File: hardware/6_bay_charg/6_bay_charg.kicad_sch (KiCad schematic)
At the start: 0 parts

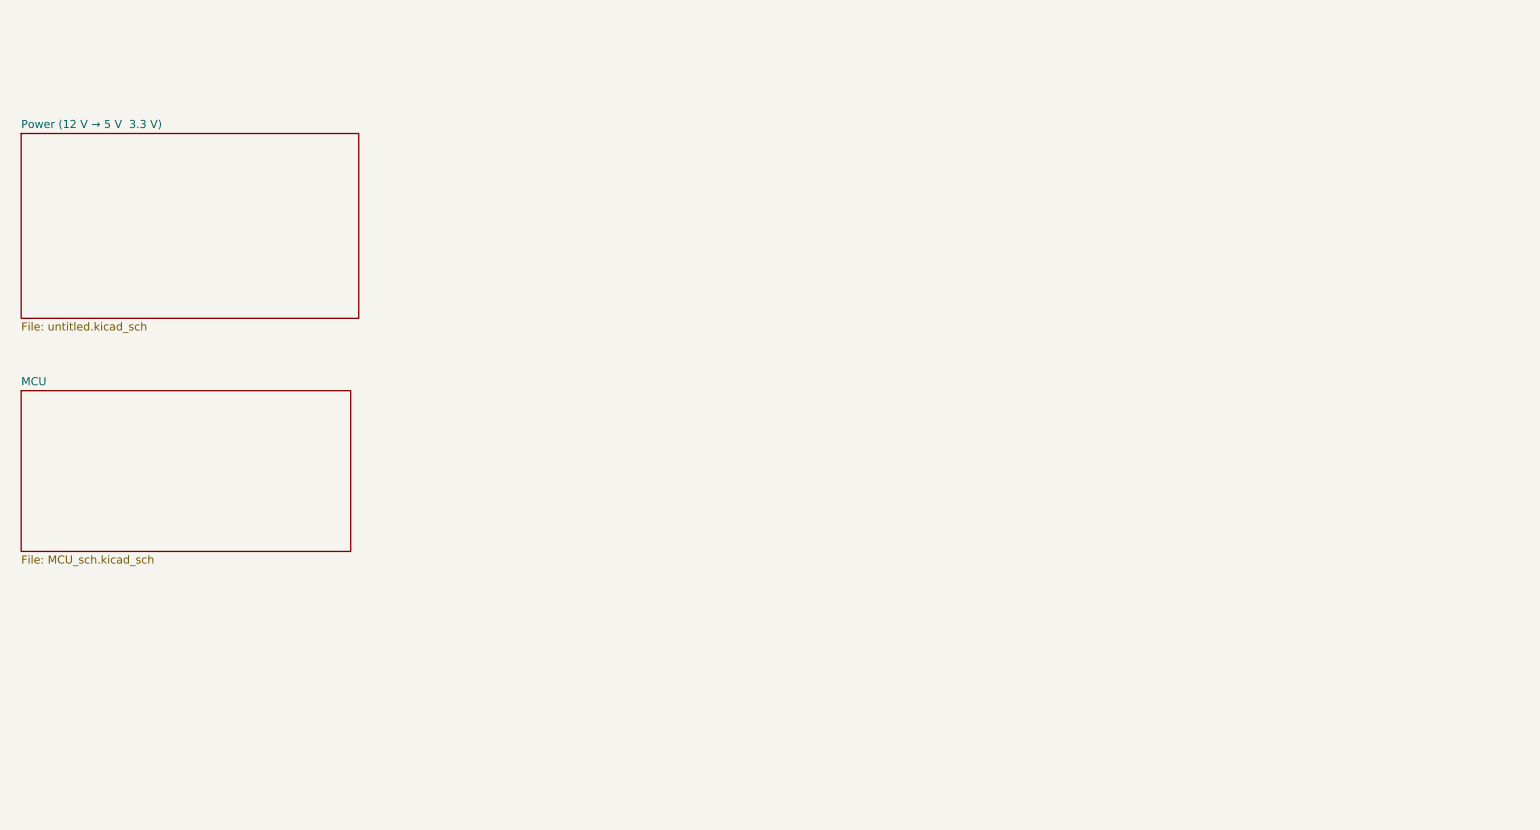
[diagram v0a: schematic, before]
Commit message: adding 3.3v buck sch + bay1
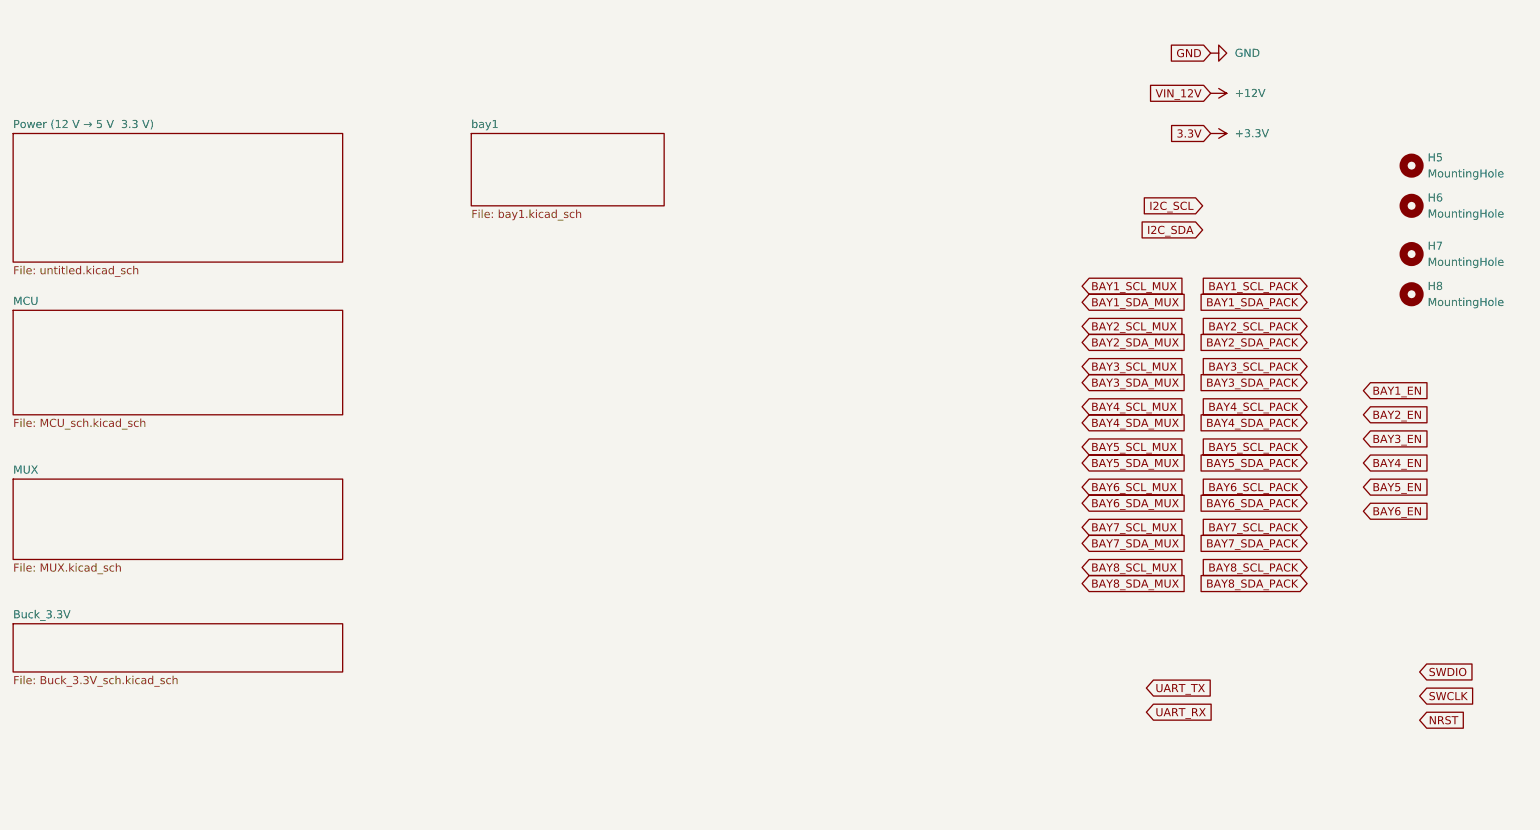
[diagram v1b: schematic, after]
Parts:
- added H5, H6, H7, H8: MountingHole, MountingHole:MountingHole_2.2mm_M2, symbol Mechanical:MountingHole
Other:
- added sheet Buck_3.3V (Buck_3.3V_sch.kicad_sch)
- added sheet MUX (MUX.kicad_sch)
- added sheet bay1 (bay1.kicad_sch)
- company: (none) -> EOS Positioning Systems

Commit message: Update KiCad schematics: dual GPIO charge/discharge per bay
- Refactored bay power control logic
- Separated GPIOs for charge and discharge paths
- Added safe idle state with hardware interlock
- Improved overall safety and control clarity
- Updated and exported schematic PDF plots
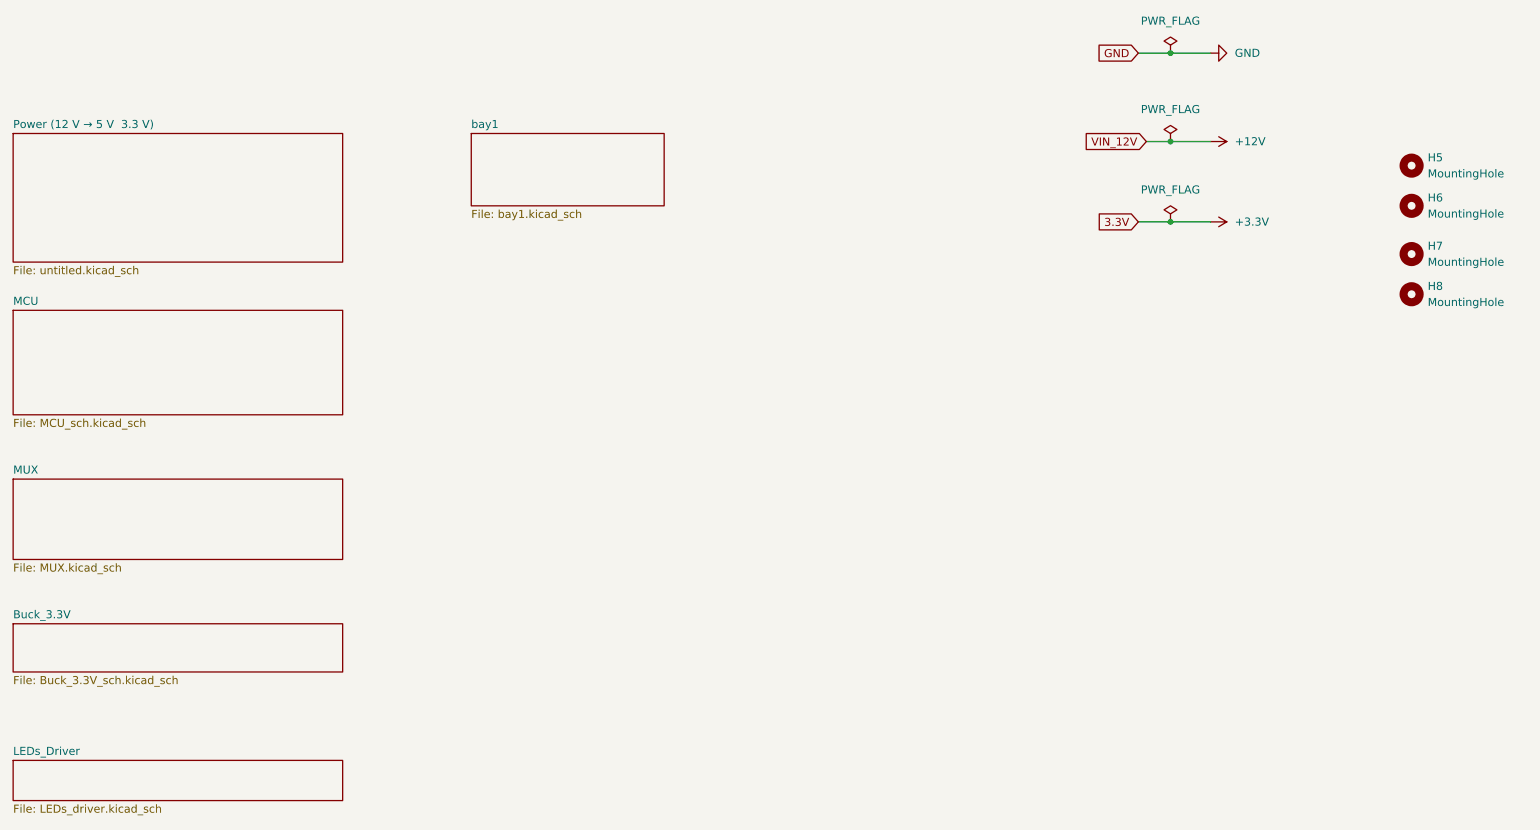
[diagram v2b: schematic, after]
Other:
- added sheet LEDs_Driver (LEDs_driver.kicad_sch)

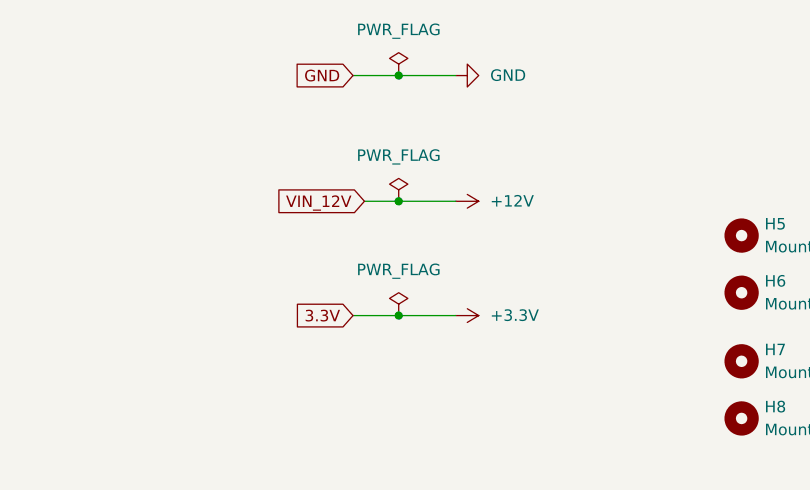
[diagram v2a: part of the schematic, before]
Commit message: Integrate fan, USB interface, firmware, and cleaned KiCad schematics
- Added 12V fan for thermal management
- Integrated USB interface (hardware and firmware)
- Added initial firmware implementation
- Cleaned and refactored KiCad schematics
- Updated and regenerated schematic PDF plots
- Updated project README to reflect latest architecture
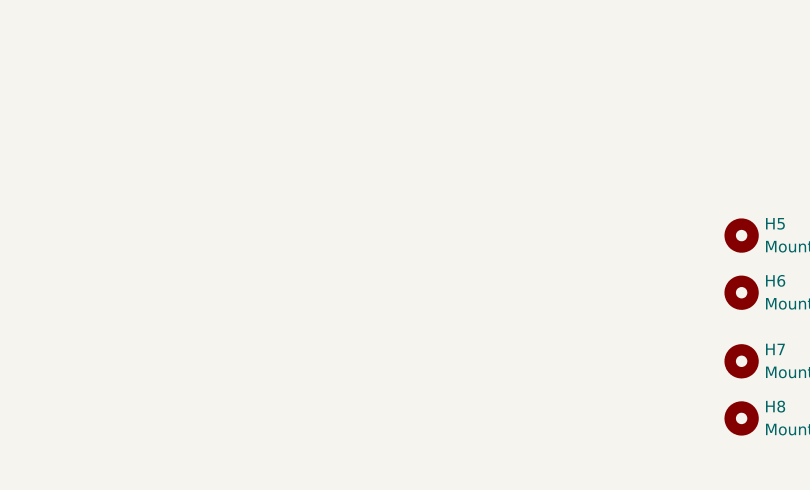
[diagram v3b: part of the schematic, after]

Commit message: update_schematics
plot last updated pdf
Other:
- sheet Power (12 V → 5 V  3.3 V) renamed Power (12 V ) + PROT +  FAN (page 2)
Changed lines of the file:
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@@
 			(color 0 0 0 0.0000)
 		)
-		(property "Sheetname" "Power (12 V → 5 V  3.3 V)"
+		(property "Sheetname" "Power (12 V ) + PROT +  FAN (page 2)"
 			(at 39.37 37.3884 0)
 			(effects

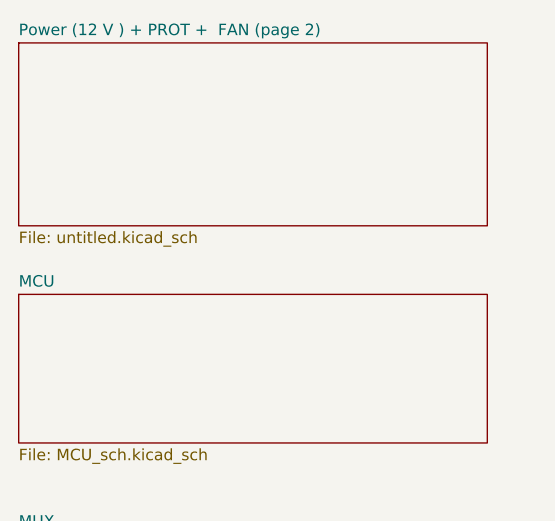
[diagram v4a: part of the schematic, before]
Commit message: updating FSM diagramme
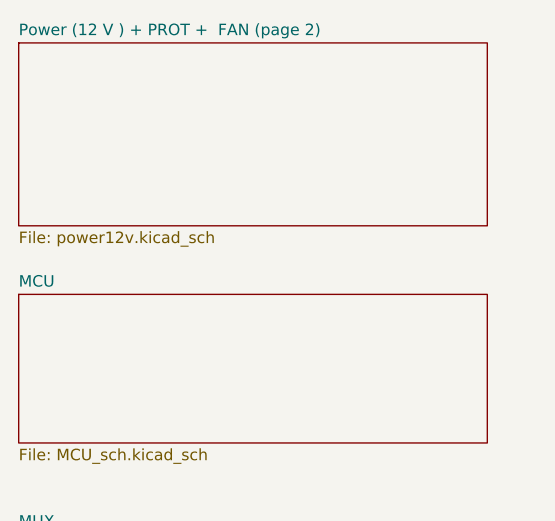
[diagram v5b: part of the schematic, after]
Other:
- sheet Power (12 V ) + PROT +  FAN (page 2): file untitled.kicad_sch -> power12v.kicad_sch
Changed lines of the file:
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@@
 			)
 		)
-		(property "Sheetfile" "untitled.kicad_sch"
+		(property "Sheetfile" "power12v.kicad_sch"
 			(at 39.37 59.0046 0)
 			(effects
